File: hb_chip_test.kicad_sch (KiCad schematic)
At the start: 141 parts, among them J1 31-5431-2010_CID2.5.196, J2 31-5431-2010_CID2.5.196, J3 31-5431-2010_CID2.5.196, J4 1945193_12P_CID2.2.928, J5 31-5431-2010_CID2.5.196, J6 31-5431-2010_CID2.5.196, U1 L7812ABD2T-TR_CID8.52.934, U2 MC7912ACD2TR4G_CID8.52.429, U3 LP2981IM5-5.0-NOPB_CID8.52.176, U5 TL084, U6 MCP3202, U7 REF5050ID, U8 Tang_Nano_9K

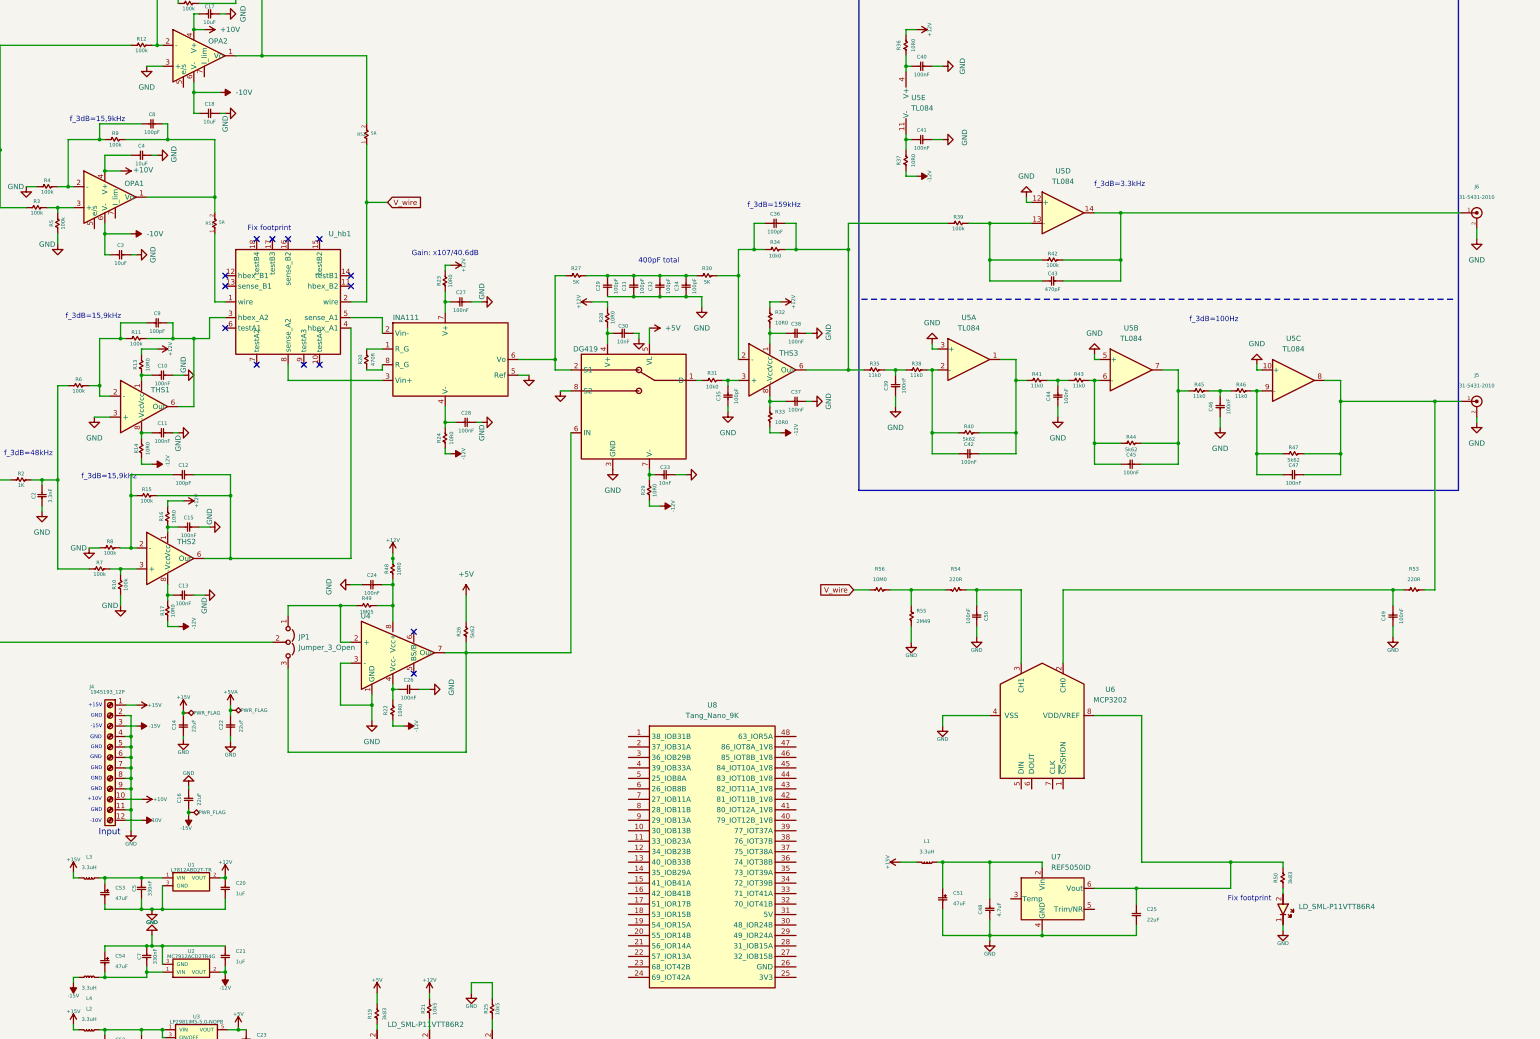
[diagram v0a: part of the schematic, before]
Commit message: Variable amps and offset circuit
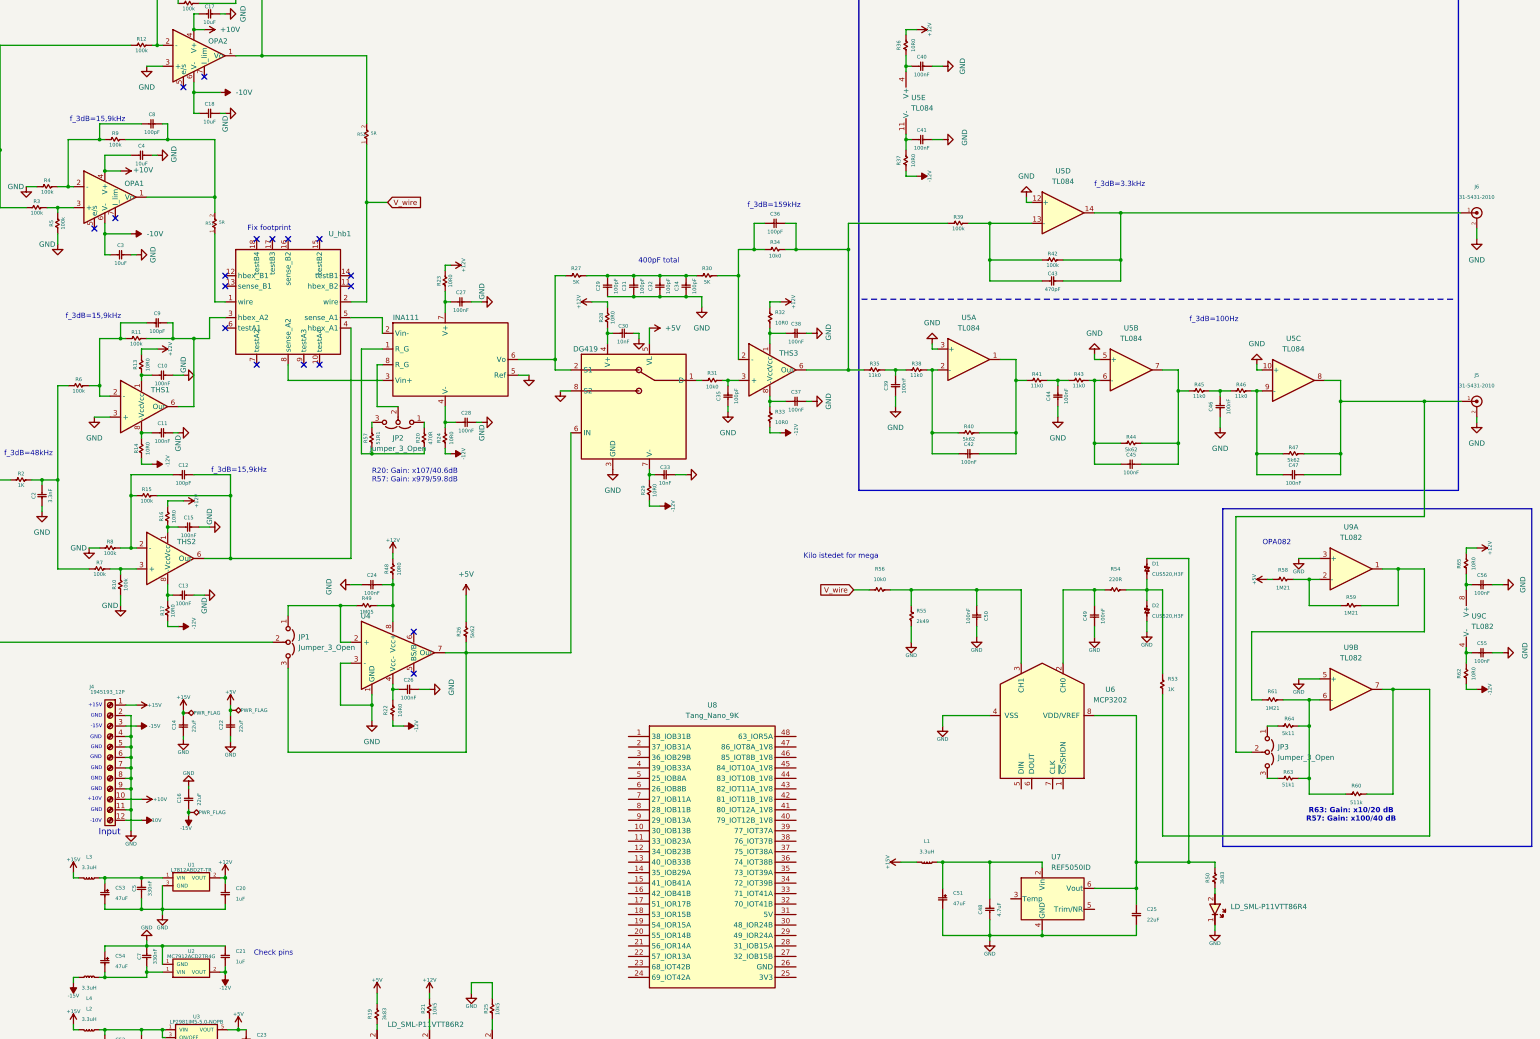
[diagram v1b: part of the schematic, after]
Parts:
- removed R53: R_0805_220R_CID10.9.602, R0805_RESC200X125X50L35N, symbol 10-Resistor:R_0805_220R_CID10.9.602
- removed R55: R_0805_2M49_CID10.9.5964, R0805_RESC200X125X50L35N, symbol 10-Resistor:R_0805_2M49_CID10.9.5964
- removed R56: R_0805_10M0_CID10.9.5993, R0805_RESC200X125X50L35N, symbol 10-Resistor:R_0805_10M0_CID10.9.5993
- added C55, C56: C_0805_100nF_16V_X7R_CID1.2.3078, C0805_CAPC200X125X130L45N, symbol 1-Capacitor:C_0805_100nF_16V_X7R_CID1.2.3078
- added D1, D2: CUS520,H3F_CID4.2.447, dtuspace:SOD250X130X120L30X30N, symbol dtuspace:CUS520,H3F_CID4.2.447
- added JP2, JP3: Jumper_3_Open, dtuspace_ipc:2_WAY_SOLDER_JUMPER, symbol Jumper:Jumper_3_Open
- added R53: R_0805_1K_CID10.99.611, R0805_RESC200X125X50L35N, symbol 10-Resistor:R_0805_1K_CID10.99.611
- added R55: R_0805_2k49_CID10.9.5859, R0805_RESC200X125X50L35N, symbol 10-Resistor:R_0805_2k49_CID10.9.5859
- added R56: R_0805_10k0_CID10.9.476, R0805_RESC200X125X50L35N, symbol 10-Resistor:R_0805_10k0_CID10.9.476
- added R57: R_0805_51R1_CID10.9.208, R0805_RESC200X125X50L35N, symbol 10-Resistor:R_0805_51R1_CID10.9.208
- added R58, R59, R61: R_0805_1M21_CID10.9.5950, R0805_RESC200X125X50L35N, symbol 10-Resistor:R_0805_1M21_CID10.9.5950
- added R60: R_0805_511k_CID10.9.489, R0805_RESC200X125X50L35N, symbol 10-Resistor:R_0805_511k_CID10.9.489
- added R62, R65: R_0805_10R0_CID10.9.4757, R0805_RESC200X125X50L35N, symbol 10-Resistor:R_0805_10R0_CID10.9.4757
- added R63: R_0805_51k1_CID10.9.5890, R0805_RESC200X125X50L35N, symbol 10-Resistor:R_0805_51k1_CID10.9.5890
- added R64: R_0805_5k11_CID10.9.467, R0805_RESC200X125X50L35N, symbol 10-Resistor:R_0805_5k11_CID10.9.467
- added U9: TL082, symbol Amplifier_Operational:TL082
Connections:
- net +5VA is gone; now on net +5V: C22.2
- net +12V: now also R65.2
- net +5V: now also R58.1
- net -12V: now also R62.1
- net GND: now also R8.1, U2.1 (VIN), C55.2, C56.2, D2.A, R55.2, U9.3 (+), U9.5 (+); no longer U2.3 (GND)
- net V_wire: now also R56.1
- net at C49.2, U6.2 (CH0): now also R54.1
- net at C47.2, J5.1, R47.2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: now also JP3.2 (C)
- net at C25.1, R50.2, U6.8 (VDD/VREF)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: now also D1.C
- net at C50.2, U6.3 (CH1): now also R55.1, R56.2; no longer R54.1
- net at R54.2: now also D1.A, D2.C, R53.2
- net at C12.1, R15.1, THS2.2 (-): now also R8.2
- net at R20.2: now also JP2.1 (A); no longer INA111.1 (R_G)
- net at INA111.8 (R_G): now also JP2.2 (C); no longer R20.1
- new net: C56.1, R65.1, U9.8 (V+)
- new net: C55.1, R62.2, U9.4 (V-)
- new net: JP2.3 (B), R57.2
- new net: JP3.1 (A), R64.1
- new net: JP3.3 (B), R63.1
- new net: R60.1, R61.2, R63.2, R64.2, U9.6 (-)
- new net: R53.1, R60.2, U9.7
- new net: R58.2, R59.1, U9.2 (-)
- new net: R59.2, R61.1, U9.1
- new net: INA111.1 (R_G), R20.1, R57.1
- no-connect marks 14 -> 18
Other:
- note added: "Check pins"
- note added: "Kilo istedet for mega"
- note added: "OPA082"
- note added: "R20: Gain: x107/40.6dB R57: Gain: x979/59.8dB"
- note added: "R63: Gain: x10/20 dB R57: Gain: x100/40 dB"
- note removed: "Gain: x107/40.6dB"
- moved on the sheet: C20, C49, LD_SML-P11VTT86R4, R20, R50

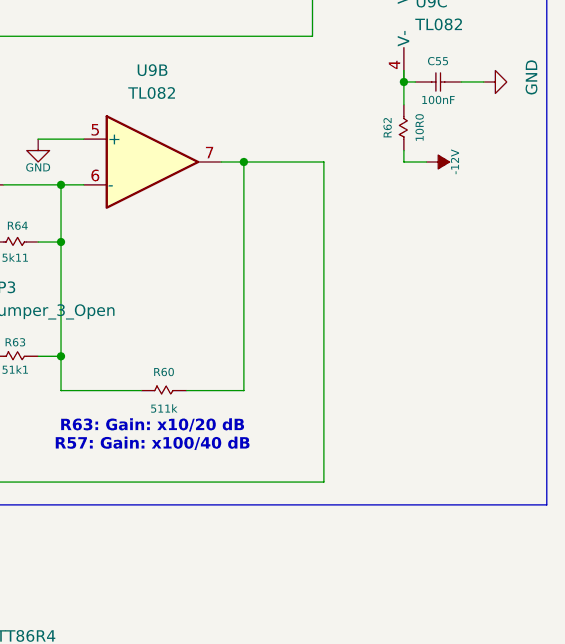
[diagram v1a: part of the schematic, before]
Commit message: BNC added
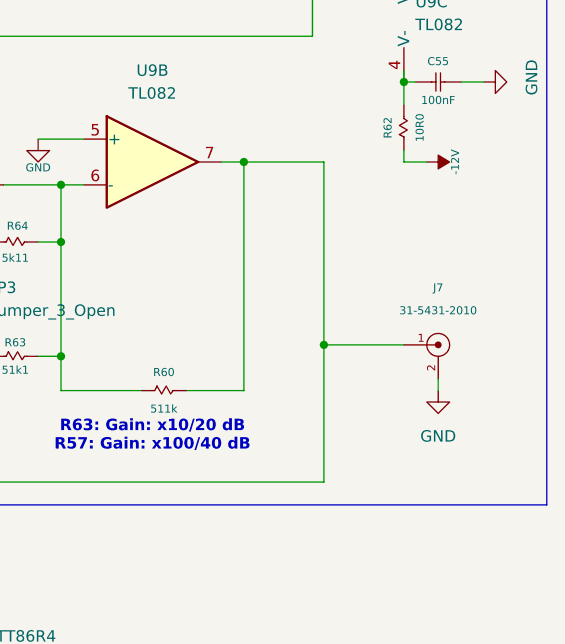
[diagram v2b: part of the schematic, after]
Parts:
- added J7: 31-5431-2010_CID2.5.196, dtuspace_ipc:AMPHENOL_31-5431-2010, symbol dtuspace:31-5431-2010_CID2.5.196
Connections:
- net GND: now also J7.2
- net at R53.1, R60.2, U9.7: now also J7.1
